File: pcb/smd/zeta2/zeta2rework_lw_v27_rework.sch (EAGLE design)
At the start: 83 parts, among them IC1 DRV8844PWPR, IC2 DRV8844PWPR, J1 B4B-ZR(LF)(SN), M1 IRLML2502, M2 IRLML2502, M3 IRLML2502, U1 STM32F427VGT7, U3 ICM-20948, U5 DS18B20U+

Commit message: using stm32f4, fixed pin settings, added cubemx
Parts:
- removed C1: 100nF, rcl:C-EUC1206
- removed C33, C38, C39, C40: 10nF, rcl:C-EUC1206
- removed C36, C37: 22pf, rcl:C-EUC1206
- removed J1: B4B-ZR(LF)(SN), B4B-ZR(LF)(SN):B4B-ZR(LF)(SN)
- removed KX-9A: 8Mhz, crystal-geyer_V1_0:KX-9A
- removed R20, R29: 10k, rcl:R-EU_R0603
- removed R30: 100k, rcl:R-EU_R0603
- removed STM32F103CB: STM32F103CB, STM32F103C8T6:STM32F103C8T6
- added C11, C12: 0pf, rcl:C-EUC1206
- added C28, C35, C41, C42, C44, C45, C46, C47, C49, C50: 100nF, rcl:C-EUC1206
- added C29, C32: 2.2µf Low ESR < 2ohm, rcl:C-EUC1206
- added C48: 4.7µf, rcl:CPOL-EUSMCP
- added C51: 1µf, rcl:C-EUC1206
- added R10, R4, R7, R8: 10k, rcl:R-EU_R0603
- added R15: 0k, rcl:R-EU_R0603
- added X1: 25mhz, crystal-geyer_V1_0:KX-9A
- C6: device rcl:C-EUC1206 -> rcl:C-EUC0603
- U1: value STM32F427VGT7 -> STM32F427VI
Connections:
- removed net FRONT_LIGHT: R6.1, STM32F103CB.PB14
- removed net INT_MD_1: J1.3, STM32F103CB.PB10
- removed net INT_MD_2: J1.2, STM32F103CB.PB11
- removed net M_DIR_L_1: STM32F103CB.PB3
- removed net M_DIR_L_2: STM32F103CB.PA15
- removed net M_DIR_R_1: STM32F103CB.PA4
- removed net M_DIR_R_2: STM32F103CB.PA5
- removed net N$46: C36.2, KX-9A.1, STM32F103CB.OSC_OUT
- removed net N$47: C37.2, KX-9A.2, STM32F103CB.OSC_IN
- removed net N$49: R30.1, STM32F103CB.PC13-TAMPER-RTC
- removed net N$5: R1.1, STM32F103CB.BOOT0
- removed net PWM_M_EN_L: STM32F103CB.PA6
- removed net PWM_M_EN_R: STM32F103CB.PA7
- removed net SCL: I2C.1, INA219.SCL, PCA9533.SCL, R29.2, STM32F103CB.PB6, U3.SCL/SCLK
- removed net SDA: I2C.2, INA219.SDA, PCA9533.SDA, R20.2, STM32F103CB.PB7, U3.SDA/SDI
- removed net U1_RX: LDIAR.1, STM32F103CB.PA10
- removed net U1_TX: LDIAR.2, STM32F103CB.PA9
- removed net USART2_RX: RPI_ZERO.34, STM32F103CB.PA3
- removed net USART2_TX: RPI_ZERO.32, STM32F103CB.PA2
- removed net USB_DM: STM32F103CB.PA11
- removed net USB_DP: STM32F103CB.PA12
- new net I2C1_SCL: INA219.SCL, PCA9533.SCL, R1.2, U1.PB6, U3.SCL/SCLK
- new net I2C1_SDA: INA219.SDA, PCA9533.SDA, R2.2, U1.PB7, U3.SDA/SDI
- new net I2C3_SCL: I2C.1, R4.2, U1.PA8
- new net I2C3_SDA: I2C.2, R10.2, U1.PC9
- new net N$13: C11.2, U1.PH1, X1.1
- new net N$14: C12.2, R15.2, X1.2
- new net N$16: R7.1, U1.BOOT0
- new net N$36: C29.2, U1.VCAP_1
- new net N$44: R15.1, U1.PH0
- new net N$45: C32.2, U1.VCAP_2
- new net PWM1: U1.PB10
- new net PWM2: U1.PB11
- new net PWM3: U1.PB0
- new net PWM4: U1.PB1
- new net PWM_LIGHT: R6.1, U1.PE9
- new net UART2_RX: U1.PA3
- new net UART2_TX: U1.PA2
- new net UART3_RX: U1.PD9
- new net UART3_TX: U1.PD8
- new net UART4_RX: RPI_ZERO.34, U1.PC11
- new net UART4_TX: RPI_ZERO.32, U1.PC10
- new net USART3_RX: LDIAR.1
- new net USART3_TX: LDIAR.2
- new net USB_OTG_DM: U1.PA11
- new net USB_OTG_DP: U1.PA12
- new net USB_OTG_ID: U1.PA10
- new net USB_OTG_VBUS: U1.PA9
- net +3V3: now also C35.1, C41.1, C42.1, C44.1, C45.1, C46.1, C47.1, C48.+, C49.1, C50.1, C51.1, R1.1, R10.1, R2.1, R4.1, R8.2, U1.VBAT, U1.VDD@1, U1.VDD@2, U1.VDD@3, U1.VDD@4, U1.VDD@5, U1.VDD@6, U1.VDDA, U1.VREF+; no longer C33.1, C38.1, C39.1, C40.1, R2.2, R20.1, R29.1, STM32F103CB.VBAT, STM32F103CB.VDD1, STM32F103CB.VDD2, STM32F103CB.VDD3, STM32F103CB.VDDA
- net +5V: no longer J1.4
- net BAT_LVL: now also U1.PC0; no longer STM32F103CB.PA0
- net DEC_LB_1: now also U1.PA6
- net DEC_LB_2: now also U1.PA7
- net DEC_LF_1: now also U1.PA0
- net DEC_LF_2: now also U1.PA1
- net DEC_RB_1: now also U1.PC6
- net DEC_RB_2: now also U1.PC7
- net DEC_RF_1: now also U1.PD12
- net DEC_RF_2: now also U1.PD13
- net GND: now also C11.1, C12.1, C28.2, C29.1, C32.1, C35.2, C41.2, C42.2, C44.2, C45.2, C46.2, C47.2, C48.-, C49.2, C50.2, C51.2, R7.2, U1.VSS@1, U1.VSS@2, U1.VSS@3, U1.VSS@4, U1.VSSA; no longer C1.2, C33.2, C36.1, C37.1, C38.2, C39.2, C40.2, J1.1, R1.2, R30.2, STM32F103CB.VSS1, STM32F103CB.VSS2, STM32F103CB.VSS3, STM32F103CB.VSSA
- net LIDAR_POS_INT: now also U1.PD0; no longer STM32F103CB.PB12
- net M_LB_IN1: now also U1.PD3
- net M_LB_IN2: now also U1.PD4
- net M_LF_IN1: now also U1.PD1
- net M_LF_IN2: now also U1.PD2
- net M_PWM_LB: now also U1.PE14
- net M_PWM_LF: now also U1.PE13
- net M_PWM_RB: now also U1.PE6
- net M_PWM_RF: now also U1.PE5
- net M_RB_IN1: now also U1.PD7
- net M_RB_IN2: now also U1.PB3
- net M_RF_IN1: now also U1.PD5
- net M_RF_IN2: now also U1.PD6
- net M_SLEEP: now also U1.PB4
- net NRST: now also C28.1, R8.1, U1.NRST; no longer C1.1, R2.1, STM32F103CB.NRST
- net PWM_FAN: now also U1.PB9; no longer STM32F103CB.PB0
- net PWM_LIDAR: now also U1.PB8; no longer STM32F103CB.PB1
- net SWCLK: now also U1.PA14; no longer STM32F103CB.PA14
- net SWDIO: now also U1.PA13; no longer STM32F103CB.PA13
- net TEMPERATURE: now also U1.PE11; no longer STM32F103CB.PB15
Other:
- moved on the sheet: 1.8V_CONV, 3.3V, 3.3V_CONV, 5V_CONV, C10, C13, C14, C15, C16, C17, C2, C21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

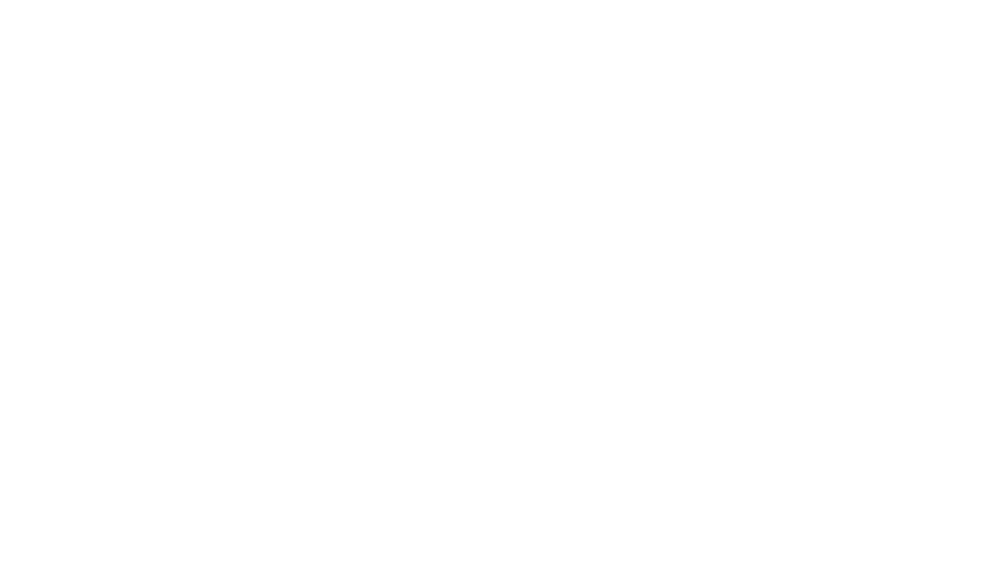
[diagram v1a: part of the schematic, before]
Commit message: added usb
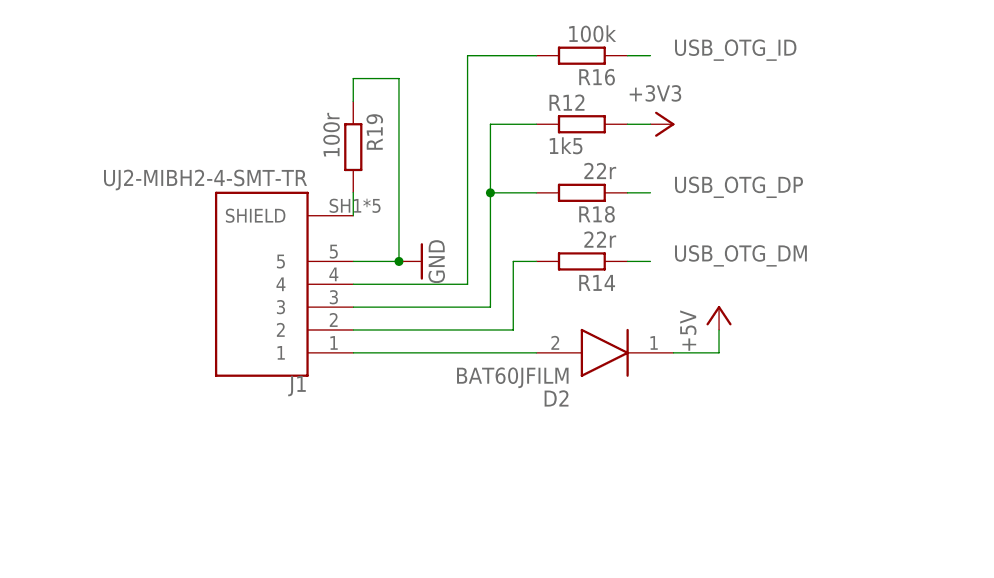
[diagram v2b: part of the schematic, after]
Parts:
- added D2: BAT60JFILM, BAT60JFILM:BAT60JFILM
- added J1: UJ2-MIBH2-4-SMT-TR, UJ2-MIBH2-4-SMT-TR:UJ2-MIBH2-4-SMT-TR
- added R12: 1k5, rcl:R-EU_R0603
- added R14, R18: 22r, rcl:R-EU_R0603
- added R16: 100k, rcl:R-EU_R0603
- added R19: 100r, rcl:R-EU_R0603
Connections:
- new net N$15: D2.A, J1.1
- new net N$17: J1.4, R16.2
- new net N$34: J1.2, R14.2
- new net N$40: J1.SHIELD, R19.2
- new net N$5: J1.3, R12.1, R18.2
- net +3V3: now also R12.2
- net +5V: now also D2.K
- net GND: now also J1.5, R19.1
- net USB_OTG_DM: now also R14.1
- net USB_OTG_DP: now also R18.1
- net USB_OTG_ID: now also R16.1
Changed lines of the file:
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@@
 <part name="R4" library="rcl" library_urn="urn:adsk.eagle:library:334" deviceset="R-EU_" device="R0603" package3d_urn="urn:adsk.eagle:package:23555/2" value="10k"/>
 <part name="R10" library="rcl" library_urn="urn:adsk.eagle:library:334" deviceset="R-EU_" device="R0603" package3d_urn="urn:adsk.eagle:package:23555/2" value="10k"/>
+<part name="J1" library="UJ2-MIBH2-4-SMT-TR" deviceset="UJ2-MIBH2-4-SMT-TR" device=""/>
+<part name="R12" library="rcl" library_urn="urn:adsk.eagle:library:334" deviceset="R-EU_" device="R0603" package3d_urn="urn:adsk.eagle:package:23555/2" value="1k5"/>
+<part name="+3V12" library="supply1" library_urn="urn:adsk.eagle:library:371" deviceset="+3V3" device=""/>
+<part name="P+3" library="supply1" library_urn="urn:adsk.eagle:library:371" deviceset="+5V" device=""/>
+<part name="D2" library="BAT60JFILM" deviceset="BAT60JFILM" device=""/>
+<part name="R14" library="rcl" library_urn="urn:adsk.eagle:library:334" deviceset="R-EU_" device="R0603" package3d_urn="urn:adsk.eagle:package:23555/2" value="22r"/>
+<part name="R16" library="rcl" library_urn="urn:adsk.eagle:library:334" deviceset="R-EU_" device="R0603" package3d_urn="urn:adsk.eagle:package:23555/2" value="100k"/>
+<part name="R18" library="rcl" library_urn="urn:adsk.eagle:library:334" deviceset="R-EU_" device="R0603" package3d_urn="urn:adsk.eagle:package:23555/2" value="22r"/>
+<part name="GND18" library="supply1" library_urn="urn:adsk.eagle:library:371" deviceset="GND" device=""/>
+<part name="R19" library="rcl" library_urn="urn:adsk.eagle:library:334" deviceset="R-EU_" device="R0603" package3d_urn="urn:adsk.eagle:package:23555/2" value="100r"/>
 </parts>
 <sheets>
@@
 <instance part="R4" gate="G$1" x="-101.6" y="-83.82" rot="R90"/>
 <instance part="R10" gate="G$1" x="-111.76" y="-88.9" rot="R90"/>
+<instance part="J1" gate="G$1" x="-515.62" y="25.4" rot="R180"/>
+<instance part="R12" gate="G$1" x="-480.06" y="43.18"/>
+<instance part="+3V12" gate="G$1" x="-469.9" y="43.18" rot="R270"/>
+<instance part="P+3" gate="1" x="-464.82" y="22.86"/>
+<instance part="D2" gate="G$1" x="-469.9" y="17.78" rot="R180"/>
+<instance part="R14" gate="G$1" x="-480.06" y="27.94" rot="R180"/>
+<instance part="R16" gate="G$1" x="-480.06" y="50.8" rot="R180"/>
+<instance part="R18" gate="G$1" x="-480.06" y="35.56" rot="R180"/>
+<instance part="GND18" gate="1" x="-497.84" y="27.94" rot="R90"/>
+<instance part="R19" gate="G$1" x="-505.46" y="40.64" rot="R270"/>
 </instances>
 <busses>
@@
 <pinref part="GND41" gate="1" pin="GND"/>
 <wire x1="-297.18" y1="27.94" x2="-297.18" y2="30.48" width="0.1524" layer="91"/>
+</segment>
+<segment>
+<pinref part="J1" gate="G$1" pin="5"/>
+<pinref part="GND18" gate="1" pin="GND"/>
+<wire x1="-505.46" y1="27.94" x2="-500.38" y2="27.94" width="0.1524" layer="91"/>
+<pinref part="R19" gate="G$1" pin="1"/>
+<wire x1="-505.46" y1="45.72" x2="-505.46" y2="48.26" width="0.1524" layer="91"/>
+<wire x1="-505.46" y1="48.26" x2="-500.38" y2="48.26" width="0.1524" layer="91"/>
+<wire x1="-500.38" y1="48.26" x2="-500.38" y2="27.94" width="0.1524" layer="91"/>
+<junction x="-500.38" y="27.94"/>
 </segment>
 </net>
@@
 <pinref part="R4" gate="G$1" pin="1"/>
 </segment>
+<segment>
+<pinref part="R12" gate="G$1" pin="2"/>
+<pinref part="+3V12" gate="G$1" pin="+3V3"/>
+<wire x1="-472.44" y1="43.18" x2="-474.98" y2="43.18" width="0.1524" layer="91"/>
+</segment>
 </net>
 <net name="+5V" class="0">
@@
 <wire x1="25.4" y1="-5.08" x2="25.4" y2="2.54" width="0.1524" layer="91"/>
 <pinref part="P+2" gate="1" pin="+5V"/>
+</segment>
+<segment>
+<wire x1="-464.82" y1="17.78" x2="-469.9" y2="17.78" width="0.1524" layer="91"/>
+<wire x1="-464.82" y1="17.78" x2="-464.82" y2="20.32" width="0.1524" layer="91"/>
+<pinref part="P+3" gate="1" pin="+5V"/>
+<pinref part="D2" gate="G$1" pin="K"/>
 </segment>
 </net>
@@
 <label x="-350.52" y="-20.32" size="1.778" layer="95"/>
 </segment>
+<segment>
+<pinref part="R18" gate="G$1" pin="1"/>
+<wire x1="-474.98" y1="35.56" x2="-472.44" y2="35.56" width="0.1524" layer="91"/>
+<label x="-469.9" y="35.56" size="1.778" layer="95"/>
+</segment>
 </net>
 <net name="USB_OTG_DM" class="0">
@@
 <label x="-350.52" y="-17.78" size="1.778" layer="95"/>
 </segment>
+<segment>
+<wire x1="-472.44" y1="27.94" x2="-474.98" y2="27.94" width="0.1524" layer="91"/>
+<label x="-469.9" y="27.94" size="1.778" layer="95"/>
+<pinref part="R14" gate="G$1" pin="1"/>
+</segment>
 </net>
 <net name="USB_OTG_ID" class="0">
@@
 <label x="-350.52" y="-15.24" size="1.778" layer="95"/>
 </segment>
+<segment>
+<wire x1="-472.44" y1="50.8" x2="-474.98" y2="50.8" width="0.1524" layer="91"/>
+<label x="-469.9" y="50.8" size="1.778" layer="95"/>
+<pinref part="R16" gate="G$1" pin="1"/>
+</segment>
 </net>
 <net name="PWM1" class="0">
@@
 </segment>
 </net>
+<net name="N$5" class="0">
+<segment>
+<pinref part="R18" gate="G$1" pin="2"/>
+<wire x1="-485.14" y1="35.56" x2="-490.22" y2="35.56" width="0.1524" layer="91"/>
+<pinref part="R12" gate="G$1" pin="1"/>
+<wire x1="-485.14" y1="43.18" x2="-490.22" y2="43.18" width="0.1524" layer="91"/>
+<wire x1="-490.22" y1="43.18" x2="-490.22" y2="35.56" width="0.1524" layer="91"/>
+<junction x="-490.22" y="35.56"/>
+<pinref part="J1" gate="G$1" pin="3"/>
+<wire x1="-505.46" y1="22.86" x2="-490.22" y2="22.86" width="0.1524" layer="91"/>
+<wire x1="-490.22" y1="22.86" x2="-490.22" y2="35.56" width="0.1524" layer="91"/>
+</segment>
+</net>
+<net name="N$15" class="0">
+<segment>
+<pinref part="D2" gate="G$1" pin="A"/>
+<wire x1="-485.14" y1="17.78" x2="-505.46" y2="17.78" width="0.1524" layer="91"/>
+<pinref part="J1" gate="G$1" pin="1"/>
+</segment>
+</net>
+<net name="N$17" class="0">
+<segment>
+<pinref part="R16" gate="G$1" pin="2"/>
+<pinref part="J1" gate="G$1" pin="4"/>
+<wire x1="-505.46" y1="25.4" x2="-492.76" y2="25.4" width="0.1524" layer="91"/>
+<wire x1="-492.76" y1="25.4" x2="-492.76" y2="50.8" width="0.1524" layer="91"/>
+<wire x1="-492.76" y1="50.8" x2="-485.14" y2="50.8" width="0.1524" layer="91"/>
+</segment>
+</net>
+<net name="N$34" class="0">
+<segment>
+<pinref part="J1" gate="G$1" pin="2"/>
+<wire x1="-505.46" y1="20.32" x2="-487.68" y2="20.32" width="0.1524" layer="91"/>
+<wire x1="-487.68" y1="20.32" x2="-487.68" y2="27.94" width="0.1524" layer="91"/>
+<pinref part="R14" gate="G$1" pin="2"/>
+<wire x1="-487.68" y1="27.94" x2="-485.14" y2="27.94" width="0.1524" layer="91"/>
+</segment>
+</net>
+<net name="N$40" class="0">
+<segment>
+<pinref part="J1" gate="G$1" pin="SHIELD"/>
+<pinref part="R19" gate="G$1" pin="2"/>
+<wire x1="-505.46" y1="33.02" x2="-505.46" y2="35.56" width="0.1524" layer="91"/>
+</segment>
+</net>

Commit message: working on new pcb layout
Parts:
- added R20: 100k, rcl:R-EU_R0603
- R11, R13, R9: value 10k -> 100k
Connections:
- new net NFAULT: IC1.NFAULT, IC2.NFAULT, R20.1, U1.PC12
- net +3V3: now also R20.2
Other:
- moved on the sheet: 3.3V, C10, C43, C6, C7, C8, D1, D2, D3, FAN, FRONTLIGHT, GND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
